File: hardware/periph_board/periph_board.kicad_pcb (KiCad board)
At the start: 2 copper layers, 149.7 x 25 mm, 45 parts, among them IC100 ADC081S021CIMF_NOPB, IC101 CD74HC4067SM96, J100 2x9 Male Pins, U200 AH49HNTR-G1, U201 AH49HNTR-G1, U202 AH49HNTR-G1, U203 AH49HNTR-G1, U204 AH49HNTR-G1, U205 AH49HNTR-G1, U206 AH49HNTR-G1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

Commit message: layout with bad adc
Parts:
- moved C100 26.4 mm to (157.7, 77.4)
- moved IC100 26.4 mm to (157.7, 80.6)
- moved IC101 26.4 mm to (151.2, 82.5)
- moved TP107 26.4 mm to (191.8, 79.7)
- moved C101 26.4 mm to (156.9, 85.3)
- moved J100 26.4 mm to (167.1, 78.5)
- moved TP101 26.4 mm to (162.8, 79.7)
- moved C206 0.36 mm to (154.7, 95.0)
- moved C209 0.36 mm to (192.8, 95.0)
- moved C201 0.36 mm to (91.2, 95.0)
- moved C202 0.36 mm to (103.9, 95.0)
- moved C200 0.36 mm to (78.5, 95.0)
- moved C203 0.36 mm to (116.6, 95.0)
- moved C204 0.36 mm to (129.3, 95.0)
- moved C205 0.36 mm to (142.0, 95.0)
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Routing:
- net +3V3: track 0.00 -> 199.5 mm, vias 0 -> 4
- net /CH0: track 0.00 -> 80.0 mm
- net /CH11: track 0.00 -> 79.3 mm
- net /CH10: track 0.00 -> 68.4 mm, vias 0 -> 2
- net /CH1: track 0.00 -> 66.4 mm
- net /CH2: track 0.00 -> 54.7 mm
- net /CH9: track 0.00 -> 52.1 mm, vias 0 -> 2
- net /S3: track 0.00 -> 49.1 mm, vias 0 -> 1
- net /S2: track 0.00 -> 45.1 mm, vias 0 -> 1
- net /CH3: track 0.00 -> 43.0 mm
- net /CH8: track 0.00 -> 37.9 mm
- net /S1: track 0.00 -> 37.4 mm
- net /CH4: track 0.00 -> 34.7 mm, vias 0 -> 2
- net /S0: track 0.00 -> 33.7 mm
- net /CH7: track 0.00 -> 33.4 mm, vias 0 -> 2
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
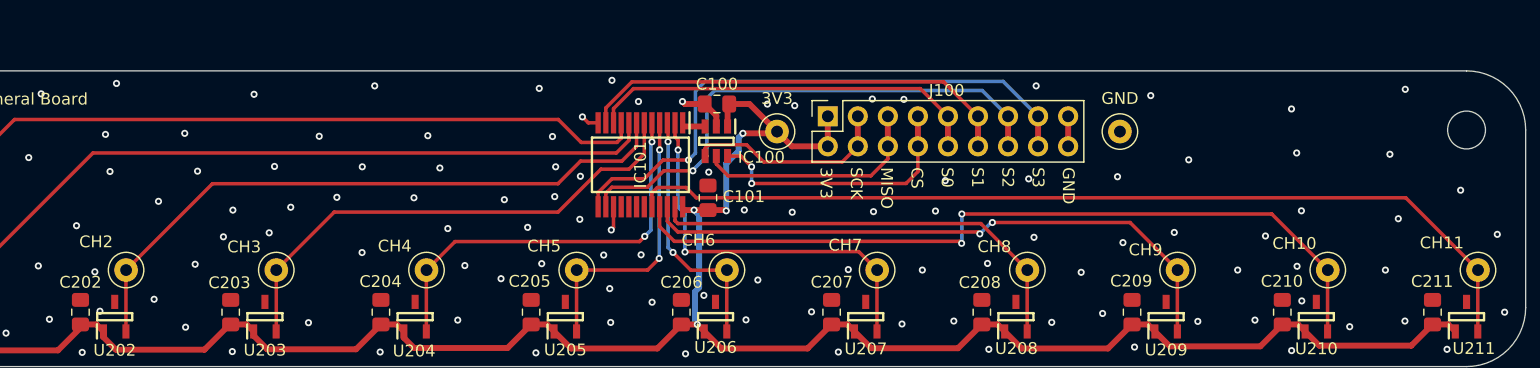
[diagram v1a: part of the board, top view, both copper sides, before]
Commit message: ece445l libraries added. moved mspm0 starter to /hw to /hardware with other files
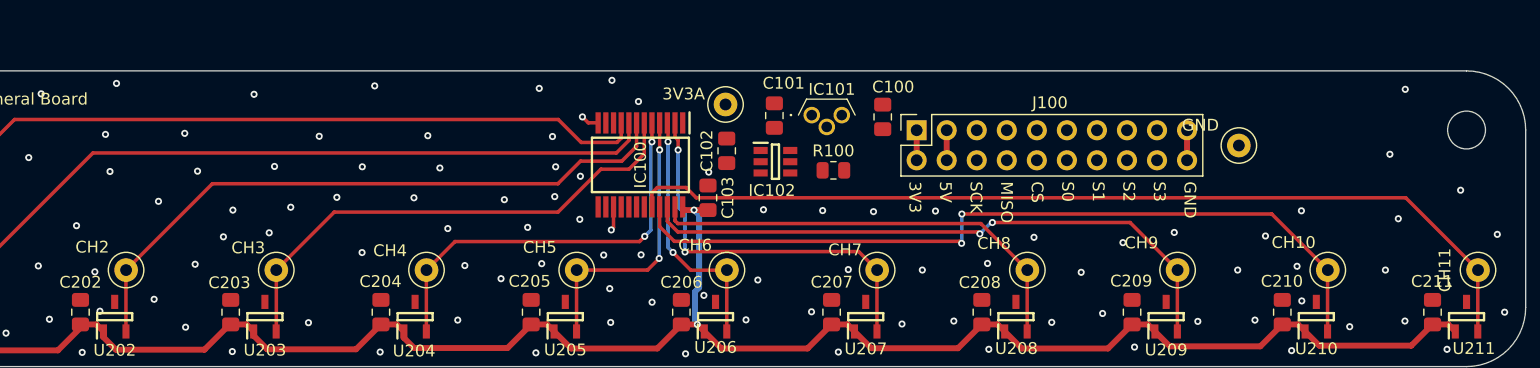
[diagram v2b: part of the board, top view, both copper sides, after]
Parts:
- removed TP101: 3V3, SamacSys_Parts:bettertestpoint2
- removed TP104: CH3, SamacSys_Parts:bettertestpoint2
- added C102: 1u, Capacitor_SMD:C_0805_2012Metric_Pad1.18x1.45mm_HandSolder, F.Cu at (158.5, 81.4)
- added C103: 1u, Capacitor_SMD:C_0805_2012Metric_Pad1.18x1.45mm_HandSolder, F.Cu at (156.9, 85.3)
- added IC102: ADC121S021CIMFX_NOPB, SamacSys_Parts:SOT95P280X145-6N, F.Cu at (162.7, 82.3)
- added R100: 100, Resistor_SMD:R_0805_2012Metric, F.Cu at (167.6, 83.0)
- added TP114: CH10, SamacSys_Parts:bettertestpoint2, F.Cu at (209.3, 91.5)
- added TP115: CH11, SamacSys_Parts:bettertestpoint2, F.Cu at (222.1, 91.5)
- IC100: value ADC081S021CIMF_NOPB -> CD74HC4067SM96; footprint SamacSys_Parts:SOT95P280X145-6N -> SamacSys_Parts:SOP65P780X200-24N
- IC101: value CD74HC4067SM96 -> LP2950-33LPRE3; footprint SamacSys_Parts:SOP65P780X200-24N -> 445L:TL431CLPM
- J100: value 2x9 Male Pins -> 2x10 Male Pins; footprint Connector_PinSocket_2.54mm:PinSocket_2x09_P2.54mm_Vertical -> Connector_PinSocket_2.54mm:PinSocket_2x10_P2.54mm_Vertical
- TP103: value CH2 -> 3V3A
- TP105: value CH4 -> CH2
- TP106: value CH5 -> CH3
- TP107: value GND -> CH4
- TP108: value CH6 -> CH5
- TP109: value CH7 -> CH6
- TP110: value CH8 -> GND
- TP111: value CH9 -> CH7
- TP112: value CH10 -> CH8
- TP113: value CH11 -> CH9
- moved TP107 59.8 mm to (133.2, 91.5), turned to 90 degrees
- moved TP103 52.6 mm to (158.4, 77.5), turned to 0 degrees
- moved TP105 25.4 mm to (107.8, 91.5)
- moved TP111 25.4 mm to (171.2, 91.5)
- moved TP112 25.4 mm to (183.9, 91.5)
- moved TP113 25.4 mm to (196.7, 91.5)
- moved TP106 25.4 mm to (120.5, 91.5)
- moved TP110 20.8 mm to (201.8, 80.9), turned to 0 degrees
- moved IC101 15.1 mm to (165.7, 78.3), turned to 0 degrees
- moved C100 14.1 mm to (171.7, 78.5), turned to 90 degrees
- moved TP108 12.7 mm to (145.8, 91.5)
- moved TP109 12.7 mm to (158.6, 91.5)
- moved C101 8.93 mm to (162.6, 78.4), turned to 90 degrees
- moved J100 7.61 mm to (174.6, 79.6)
- moved IC100 6.72 mm to (151.2, 82.6)
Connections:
- C100 pad 2: +3V3 -> +5V
- C101 pad 2: +3V3 -> +3.3VADC
- IC100 pad 1: +3V3 -> /HALL_OUT
- IC100 pad 2: GND -> /CH7
- IC100 pad 3: /HALL_OUT -> /CH6
- IC100 pad 4: /SCK -> /CH5
- IC100 pad 5: /MISO -> /CH4
- IC100 pad 6: /CS -> /CH3
- IC101 pad 1: /HALL_OUT -> +3.3VADC
- IC101 pad 2: /CH7 -> GND
- IC101 pad 3: /CH6 -> +5V
- J100 pad 10: /S0 -> /CS
- J100 pad 11: /S1 -> /S0
- J100 pad 12: /S1 -> /S0
- J100 pad 13: /S2 -> /S1
- J100 pad 14: /S2 -> /S1
- J100 pad 15: /S3 -> /S2
- J100 pad 16: /S3 -> /S2
- J100 pad 17: GND -> /S3
- J100 pad 18: GND -> /S3
- J100 pad 3: /SCK -> +5V
- J100 pad 4: /SCK -> +5V
- J100 pad 5: /MISO -> /SCK
- J100 pad 6: /MISO -> /SCK
- J100 pad 7: /CS -> /MISO
- J100 pad 8: /CS -> /MISO
- J100 pad 9: /S0 -> /CS
- TP103 pad 1: /CH2 -> +3.3VADC
- TP105 pad 1: /CH4 -> /CH2
- TP106 pad 1: /CH5 -> /CH3
- TP107 pad 1: GND -> /CH4
- TP108 pad 1: /CH6 -> /CH5
- TP109 pad 1: /CH7 -> /CH6
- TP110 pad 1: /CH8 -> GND
- TP111 pad 1: /CH9 -> /CH7
- TP112 pad 1: /CH10 -> /CH8
- TP113 pad 1: /CH11 -> /CH9
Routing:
- net /S3: track 49.1 -> 0.00 mm, vias 1 -> 0
- net /S2: track 45.1 -> 0.00 mm, vias 1 -> 0
- net /S1: track 37.4 -> 0.00 mm
- net /S0: track 33.7 -> 0.00 mm
- net +3V3: track 199.5 -> 176.1 mm, vias 4 -> 2
- net /CS: track 23.0 -> 0.00 mm, vias 2 -> 0
- net /MISO: track 19.8 -> 0.00 mm
- net /SCK: track 17.4 -> 0.00 mm
- net GND: track 10.4 -> 6.12 mm, vias 128 -> 115
- net +5V: track 0.00 -> 2.54 mm
- net /HALL_OUT: track 1.84 -> 0.00 mm
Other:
- board text added: "5V"

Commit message: third peripheral board layout done
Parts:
- moved C101 1.25 mm to (161.9, 79.4)
- moved C100 1.16 mm to (171.0, 79.4)
- moved IC102 0.91 mm to (162.6, 83.2)
- moved C102 0.90 mm to (159.4, 81.5)
- moved IC101 0.73 mm to (165.2, 77.9)
- moved TP103 0.31 mm to (158.4, 77.8)
- moved R100 0.26 mm to (167.4, 83.2)
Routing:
- net /S3: track 0.00 -> 61.0 mm, vias 0 -> 1
- net /S2: track 0.00 -> 56.8 mm, vias 0 -> 1
- net /S1: track 0.00 -> 48.6 mm
- net /S0: track 0.00 -> 44.3 mm
- net /CS: track 0.00 -> 28.8 mm, vias 0 -> 2
- net /SCK: track 0.00 -> 21.0 mm, vias 0 -> 3
- net +3V3: track 176.1 -> 197.0 mm, vias 2 -> 4
- net /MISO: track 0.00 -> 17.4 mm, vias 0 -> 2
- net +3.3VADC: track 0.00 -> 13.0 mm
- net +5V: track 2.54 -> 13.5 mm
- net /HALL_OUT: track 0.00 -> 9.20 mm
- net GND: track 6.12 -> 10.1 mm, vias 115 -> 139
- net Net-(IC102-SDATA): track 0.00 -> 2.61 mm
